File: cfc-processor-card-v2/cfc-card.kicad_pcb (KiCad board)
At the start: 4 copper layers, 99.8 x 94.6 mm, 268 parts, among them J1 ORESAT-DEBUG-CONNECTOR-ALL, J100 DM3BT-DSF-PEJS, J2 J-SAMTEC-TFM-110-X1-XXX-D-RA, J3 CONN_03LONGPADS, J4 TFM-120-01-L-D-RA, Q1 MMBT2907, Q2 PMV45EN, Q3 DMP2240UDM, Q4 PMV45EN, Q5 MOSFET-PCH-SOT23-6, Q6 MOSFET-PCH-SOT23-6, U1 RCLAMP0504FB, U10 TLVH431, U11 TCAN330, U12 MIC842LYC5, U13 MIC842LYC5, U14 MAX4211FETE, U15 TPS62112, U16 MAX7310ATE, U2 DS90CR218AMTD/NOPBMTD48_TEX-L, U3 THGBMJG7C2LBAU8, U4 SN74LVC1G07DCK, U5 TS5A21366, U7 OSD3358-512M-BSM, Y1 24MHz, Y2 ABS07-32.768KHZ-T

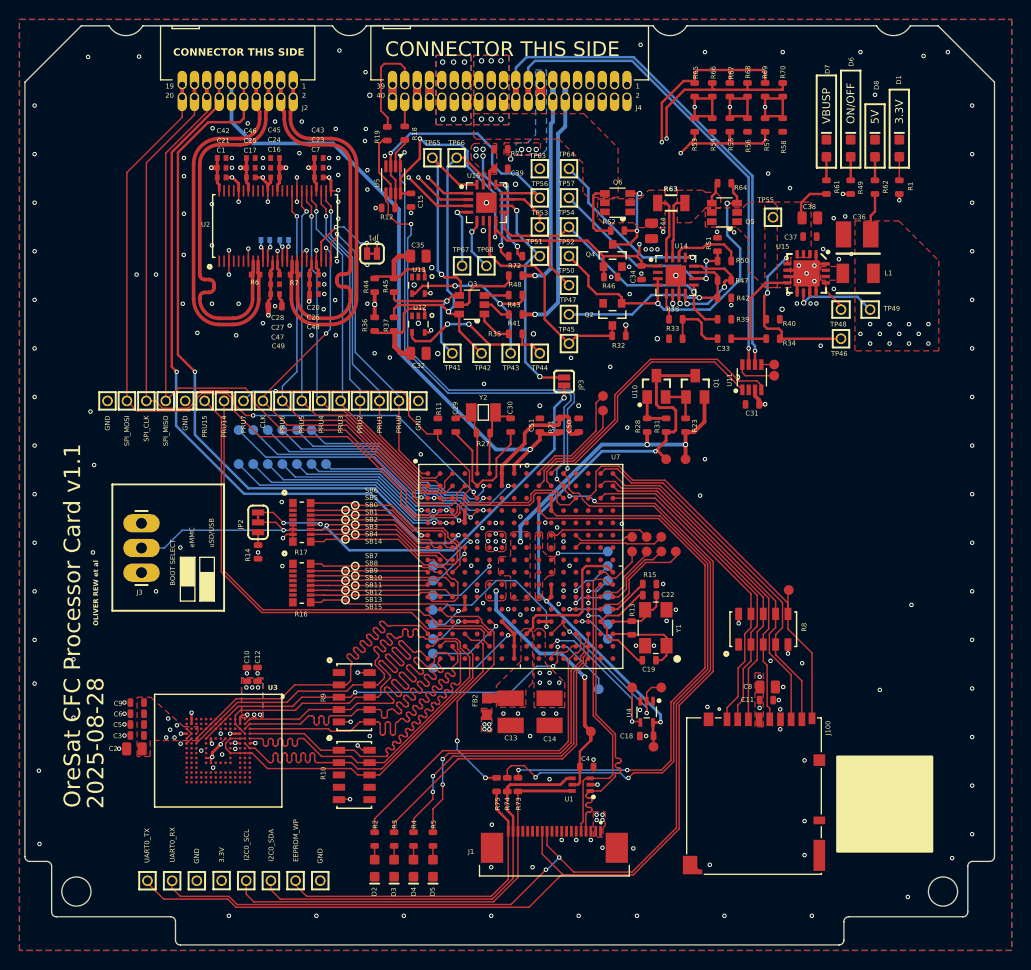
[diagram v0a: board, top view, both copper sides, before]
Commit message: Final polish on schematic and PCB. Cleaned up BOM, fixed github issues which were not really issues. Lots of BOM cleanup, with MPNs and DPNs.
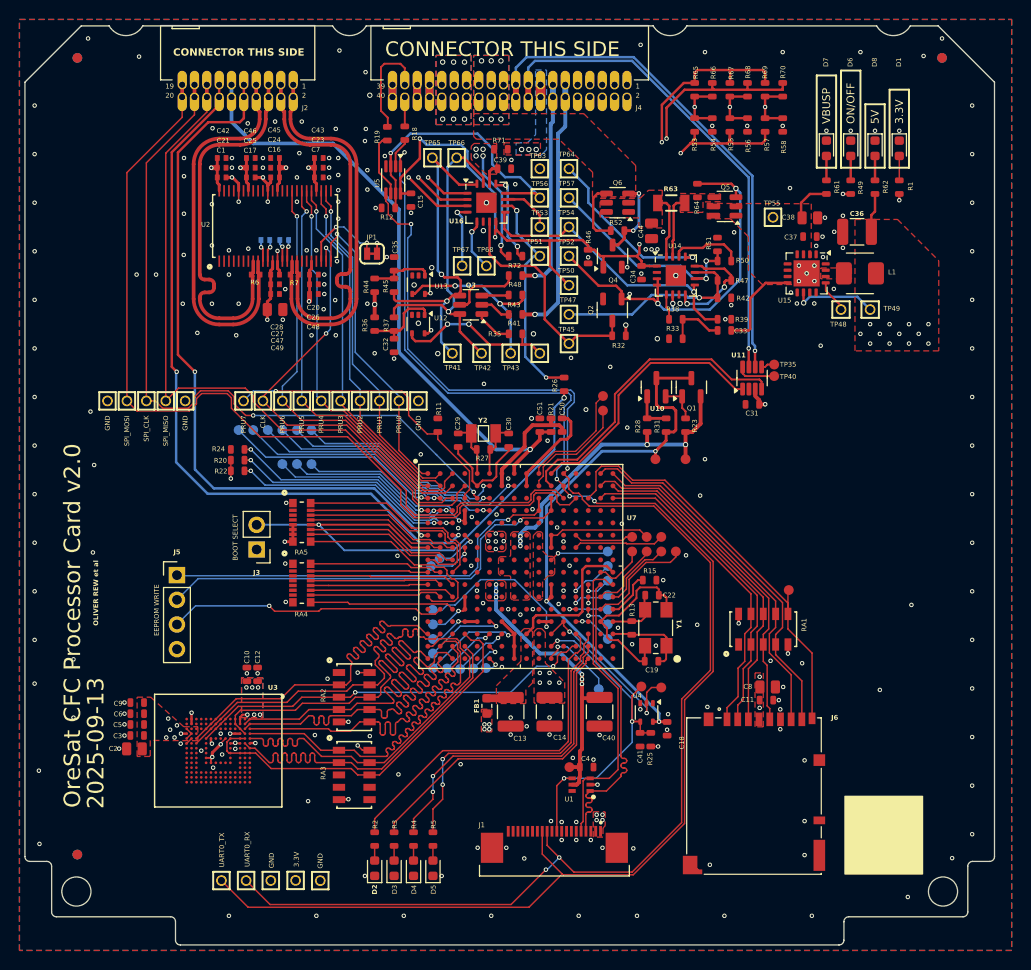
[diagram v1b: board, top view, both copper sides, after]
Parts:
- removed JP2: JUMPER-SMT_3_1-NC_TRACE_SILK, cfc-card:SMT-JUMPER_3_1-NC_TRACE_SILK
- removed JP3: JUMPER-SMT_2_NO_SILK, cfc-card:SMT-JUMPER_2_NO_SILK
- removed R14: DNP, oresat-passives:0603-C-NOSILK
- removed R34: 10k, oresat-passives:0603-C-NOSILK
- removed R40: NP, oresat-passives:0603-C-NOSILK
- removed R73, R74, R75: 100, oresat-passives:0603-C-NOSILK
- removed SB0, SB1, SB10, SB11, SB12, SB13, SB14, SB15, SB2, SB3, SB4, SB5, SB6, SB7, SB8, SB9: TEST-POINT-SMALL, cfc-card:TEST-POINT-SMALL
- removed TP157, TP173: TEST-POINT3X4, cfc-card:PAD.03X.04
- removed TP33, TP34, TP39, TP46, TP70, TP71: TEST-POINT, cfc-card:2MM-TEST-POINT
- added C40: 22u, Capacitor_SMD:C_1210_3225Metric, F.Cu at (157.8, 128.3)
- added C41: 100n, oresat-passives:0603-C-NOSILK, F.Cu at (161.9, 131.2)
- added FID1: Fiducial, Fiducial:Fiducial_1mm_Mask2mm, F.Cu at (104.0, 61.0)
- added FID2: Fiducial, Fiducial:Fiducial_1mm_Mask2mm, F.Cu at (104.0, 143.0)
- added FID3: Fiducial, Fiducial:Fiducial_1mm_Mask2mm, F.Cu at (193.0, 61.0)
- added FID4: Fiducial, Fiducial:Fiducial_1mm_Mask2mm, B.Cu at (104.0, 143.0)
- added FID5: Fiducial, Fiducial:Fiducial_1mm_Mask2mm, B.Cu at (104.0, 61.0)
- added FID6: Fiducial, Fiducial:Fiducial_1mm_Mask2mm, B.Cu at (193.0, 61.0)
- added J5: Conn_01x04, Connector_PinHeader_2.54mm:PinHeader_1x04_P2.54mm_Vertical, F.Cu at (114.2, 114.2)
- added R20: 10k, oresat-passives:0603-C-NOSILK, F.Cu at (120.5, 102.4)
- added R22: 10k, oresat-passives:0603-C-NOSILK, F.Cu at (120.5, 103.5)
- added R24: 10k, oresat-passives:0603-C-NOSILK, F.Cu at (120.5, 101.3)
- added R25: 10k, oresat-passives:0603-C-NOSILK, F.Cu at (163.0, 131.2)
- added R26: 10k, oresat-passives:0603-C-NOSILK, F.Cu at (154.1, 94.6)
- C10, C12, C3, C33, C34, C37, C5, C6, C9: value 1uF -> 1u
- C11, C18, C31, C39, C50: value 0.1uF -> 100n
- C13, C14, C36: value 22uF -> 22u; footprint cfc-card:C1210 -> Capacitor_SMD:C_1210_3225Metric
- C19, C22: value 18pF, 50V -> 10p
- C2, C38, C44, C8: value 10uF -> 10u
- C29, C30: value 18pF, 50V -> 18p
- C32, C35: value 1uF -> 1u; footprint oresat-passives:0805-C-NOSILK -> oresat-passives:0603-C-NOSILK
- C49: footprint oresat-passives:0603-C-NOSILK -> oresat-passives:0805-C-NOSILK
- C51: value 0.1u -> 100n
- D1, D2, D3, D4, D5, D6, D7, D8: footprint cfc-card:LED-0603 -> LED_SMD:LED_0603_1608Metric
- FB1: renamed from FB2; value 30Ω/1.8A -> BLM18KG300JH1D; footprint cfc-card:0603 -> Inductor_SMD:L_0603_1608Metric
- J1: value ORESAT-DEBUG-CONNECTOR-ALL -> 2-1734592-0
- J3: value CONN_03LONGPADS -> Conn_01x02; footprint cfc-card:1X03_LONGPADS -> Connector_PinHeader_2.54mm:PinHeader_1x02_P2.54mm_Vertical
- J6: renamed from J100; footprint cfc-card:DM3BT-DSF-PEJS -> oresat-connectors:J-Hirose-DM3BT-DSF-PEJS
- L1: footprint cfc-card:ECS-MPI4040 -> oresat-passives:L_ECS-MPI4040
- Q1: footprint cfc-card:SOT23-BEC -> Package_TO_SOT_SMD:SOT-23
- Q2, Q4: footprint cfc-card:SOT23 -> Package_TO_SOT_SMD:SOT-23-3
- Q3: footprint cfc-card:SOT23-6 -> Package_TO_SOT_SMD:SOT-23-6
- Q5, Q6: value MOSFET-PCH-SOT23-6 -> DMP3050LVT-7; footprint cfc-card:SOT23-6 -> Package_TO_SOT_SMD:TSOT-23-6
- R11: value DNP -> 10k
- R27: value DNP -> 1M
- R29, R30: value NP -> 100
- R42: value NP -> 10k
- RA4: renamed from R16; value 100k -> 47k
- RA5: renamed from R17; value 100k -> 47k
- TP14: moved to B.Cu
- U10: footprint cfc-card:SOT23-3 -> Package_TO_SOT_SMD:SOT-23
- U11: footprint cfc-card:SOT23-8_TI-DCN -> Package_TO_SOT_SMD:SOT-23-8
- U12, U13: footprint cfc-card:SC70-5 -> Package_TO_SOT_SMD:SOT-353_SC-70-5
- U14: footprint cfc-card:QFN65P400X400X80-17T210 -> Package_DFN_QFN:QFN-16-1EP_4x4mm_P0.65mm_EP2.1x2.1mm
- U15: footprint cfc-card:S-PVQFN-16 -> Package_DFN_QFN:Texas_RSA_VQFN-16-1EP_4x4mm_P0.65mm_EP2.7x2.7mm
- U16: value MAX7310ATE -> MAX7310ATE+; footprint cfc-card:QFN65P400X400X80-17T210 -> Package_DFN_QFN:QFN-16-1EP_4x4mm_P0.65mm_EP2.1x2.1mm
- U2: value DS90CR218AMTD/NOPBMTD48_TEX-L -> DS90CR218AMTD/NOPB
- U3: value THGBMJG7C2LBAU8 -> SFEM016GB1EA1TO-I-GE-121-STD
- U4: value SN74LVC1G07DCK -> SN74AUC1G07DCKR; footprint cfc-card:C70(TI-DCK) -> Package_TO_SOT_SMD:SOT-353_SC-70-5
- U7: value OSD3358-512M-BSM -> OSD3358-1G-ISM; footprint cfc-card:OSD335X-BGA-256 -> oresat-ics:U-Octavo-OSD335X-BGA-256
- Y1: value 24MHz -> ECS-240-12-30BQ-AEN-TR; footprint cfc-card:5X3.2-4SMD -> oresat-passives:CRYSTAL-5X3.2-4SMD
- Y2: footprint cfc-card:CRYSTAL_3.2X1.5 -> oresat-passives:CRYSTAL_3.2X1.5
- moved TP10 32.0 mm to (144.8, 123.8), turned to 0 degrees
- moved TP11 31.8 mm to (146.1, 123.8), turned to 0 degrees
- moved TP9 28.0 mm to (142.1, 123.8), turned to 0 degrees
- moved TP14 21.4 mm to (143.4, 123.9), turned to 0 degrees
- moved J3 12.2 mm to (122.5, 111.6), turned to 180 degrees
- moved TP32 7.61 mm to (118.8, 145.7)
- moved TP78 7.61 mm to (123.9, 145.7)
- moved TP2 7.61 mm to (126.5, 145.7)
- moved TP31 7.61 mm to (121.4, 145.7)
- moved TP3 4.27 mm to (154.7, 134.0)
- moved R46 3.13 mm to (156.6, 81.5), turned to 90 degrees
- moved R64 2.88 mm to (167.8, 74.7), turned to -90 degrees
- moved C32 2.63 mm to (136.6, 90.6), turned to -90 degrees
- moved C35 2.62 mm to (136.6, 82.2), turned to 90 degrees
- moved C18 2.23 mm to (164.7, 130.1), turned to -90 degrees
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- renumbered R8 to RA1, R9 to RA2, R10 to RA3
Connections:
- net /OSD3358: SIP A + E + F (PWR)/PMIC_PGOOD renamed /OSD3358: SIP A (PWR)/PMIC_PGOOD
- net /OSD3358: SIP C (SD, eMMC)/EMMC_CLK renamed /OSD3358: SIP C (SD, eMMC, PRU)/EMMC_CLK
- net /OSD3358: SIP C (SD, eMMC)/EMMC_CMD renamed /OSD3358: SIP C (SD, eMMC, PRU)/EMMC_CMD
- net /OSD3358: SIP C (SD, eMMC)/PRU_BUS.PRU0_0 renamed /OSD3358: SIP C (SD, eMMC, PRU)/PRU_BUS.PRU0_0
- net /OSD3358: SIP C (SD, eMMC)/PRU_BUS.PRU0_1 renamed /OSD3358: SIP C (SD, eMMC, PRU)/PRU_BUS.PRU0_1
- net /OSD3358: SIP C (SD, eMMC)/PRU_BUS.PRU0_2 renamed /OSD3358: SIP C (SD, eMMC, PRU)/PRU_BUS.PRU0_2
- net /OSD3358: SIP C (SD, eMMC)/PRU_BUS.PRU0_3 renamed /OSD3358: SIP C (SD, eMMC, PRU)/PRU_BUS.PRU0_3
- net /OSD3358: SIP C (SD, eMMC)/PRU_BUS.PRU0_4 renamed /OSD3358: SIP C (SD, eMMC, PRU)/PRU_BUS.PRU0_4
- net /OSD3358: SIP C (SD, eMMC)/PRU_BUS.PRU0_5 renamed /OSD3358: SIP C (SD, eMMC, PRU)/PRU_BUS.PRU0_5
- net /OSD3358: SIP C (SD, eMMC)/PRU_BUS.PRU0_6 renamed /OSD3358: SIP C (SD, eMMC, PRU)/PRU_BUS.PRU0_6
- net /OSD3358: SIP C (SD, eMMC)/PRU_BUS.PRU0_7 renamed /OSD3358: SIP C (SD, eMMC, PRU)/PRU_BUS.PRU0_7
- net /OSD3358: SIP C (SD, eMMC)/PRU_BUS.PRU_16_CLK renamed /OSD3358: SIP C (SD, eMMC, PRU)/PRU_BUS.PRU_16_CLK
- net /OSD3358: SIP C (SD, eMMC)/~{EMMC_RST} renamed /OSD3358: SIP C (SD, eMMC, PRU)/~{EMMC_RST}
- net /Power (OPD)/BOOT0 renamed Net-(U16-IO5)
- net Net-(R10-11) renamed /OSD3358: SIP C (SD, eMMC, PRU)/EMMC_D1
- net Net-(R10-22) renamed /OSD3358: SIP C (SD, eMMC, PRU)/EMMC_D7
- net Net-(R10-88) renamed /OSD3358: SIP C (SD, eMMC, PRU)/EMMC_D6
- net Net-(R10-99) renamed /OSD3358: SIP C (SD, eMMC, PRU)/EMMC_D2
- net Net-(R9-44) renamed /OSD3358: SIP C (SD, eMMC, PRU)/EMMC_D3
- net Net-(R9-66) renamed /OSD3358: SIP C (SD, eMMC, PRU)/EMMC_D0
- net Net-(R9-77) renamed /OSD3358: SIP C (SD, eMMC, PRU)/EMMC_D4
- net Net-(R9-88) renamed /OSD3358: SIP C (SD, eMMC, PRU)/EMMC_D5
- net Net-(U7A-I2C0_SCL) renamed /OSD3358: SIP A (PWR)/I2C0_SCL
- net Net-(U7A-I2C0_SDA) renamed /OSD3358: SIP A (PWR)/I2C0_SDA
- C18 pad 1: /OSD3358: SIP A + E + F (PWR)/N$118 -> Net-(Q1-C)
- C50 pad 2: GND -> Net-(U7B-AGND_ADC)
- J1 pad 10: unconnected-(J1-NRST-Pad10) -> nRESET
- J1 pad 18: I2C0_SCL -> unconnected-(J1-DEBUG-1-Pad18)
- J1 pad 19: I2C0_SDA -> unconnected-(J1-DEBUG-2-Pad19)
- J1 pad 20: EEPROM_WP -> unconnected-(J1-DEBUG-3-Pad20)
- J3 pad 1: 3.3V -> GND
- R1 pad 2: Net-(D1-PadA) -> Net-(D1-A)
- R2 pad 2: Net-(D2-PadA) -> Net-(D2-A)
- R23 pad 1: Net-(U10-CATHODE) -> Net-(Q1-B)
- R3 pad 2: Net-(D3-PadA) -> Net-(D3-A)
- R31 pad 1: /OSD3358: SIP A + E + F (PWR)/N$118 -> Net-(Q1-C)
- R4 pad 2: Net-(D4-PadA) -> Net-(D4-A)
- R49 pad 1: Net-(D6-PadA) -> Net-(D6-A)
- R5 pad 2: Net-(D5-PadA) -> Net-(D5-A)
- R61 pad 1: Net-(D7-PadA) -> Net-(D7-A)
- R62 pad 1: Net-(D8-PadA) -> Net-(D8-A)
- RA5 pad 12: Net-(JP2-Pad3) -> SYSBOOT2
- TP109 pad P$1: /OSD3358: SIP A + E + F (PWR)/RESET# -> nRESET
- TP14 pad P$1: /OSD3358: SIP A + E + F (PWR)/N$118 -> Net-(TP14-1)
- TP164 pad P$1: /OSD3358: SIP A + E + F (PWR)/N$118 -> Net-(Q1-C)
- U1 pad 4: I2C0_SDA -> nRESET
- U1 pad 6: I2C0_SCL -> unconnected-(U1-I4-Pad6)
- U10 pad 2: Net-(U10-CATHODE) -> Net-(Q1-B)
- U10 pad 3: /OSD3358: SIP A + E + F (PWR)/N$118 -> Net-(Q1-C)
- U12 pad 3: (no net) -> unconnected-(U12-Pad3)
- U13 pad 3: (no net) -> unconnected-(U13-Pad3)
- U14 pad 2: (no net) -> unconnected-(U14-IN_(NC)-Pad2)
- U15 pad 5: Net-(U15-SYNC) -> GND
- U2 pad 6: (no net) -> unconnected-(U2-Pad6)
- U4 pad 1: (no net) -> unconnected-(U4-Pad1)
- U4 pad 4: /OSD3358: SIP A + E + F (PWR)/RESET# -> nRESET
- U4 pad 5: /OSD3358: SIP A + E + F (PWR)/N$118 -> Net-(Q1-C)
- U7 pad A9: GND -> Net-(U7B-AGND_ADC)
- U7 pad B9: GND -> Net-(U7B-AGND_ADC)
- U7 pad D3: Net-(TP9-1) -> Net-(U7B-TRSTN)
- U7 pad D5: Net-(TP173-1) -> unconnected-(U7F-CAP_VDD_RTC-PadD5)
- U7 pad E2: Net-(TP10-1) -> Net-(U7B-EMU0)
- U7 pad E3: Net-(TP11-1) -> Net-(U7B-EMU1)
- U7 pad H6: Net-(TP157-1) -> unconnected-(U7F-VPP-PadH6)
- U7 pad K11: /OSD3358: SIP A + E + F (PWR)/N$118 -> Net-(Q1-C)
- U7 pad L11: /OSD3358: SIP A + E + F (PWR)/N$118 -> Net-(Q1-C)
- U7 pad M2: Net-(U7A-EEPROM_WP) -> /OSD3358: SIP A (PWR)/EEPROM_WP
- U7 pad P6: /OSD3358: SIP C (SD, eMMC)/PRU_BUS.PRU0_14 -> Net-(TP9-1)
- U7 pad P7: unconnected-(U7C-GPMC_AD15-PadP7) -> Net-(TP14-1)
- U7 pad R11: /OSD3358: SIP A + E + F (PWR)/RESET# -> nRESET
- U7 pad R6: /OSD3358: SIP C (SD, eMMC)/PRU_BUS.PRU0_15 -> Net-(TP10-1)
- U7 pad T6: unconnected-(U7C-GPMC_AD14-PadT6) -> Net-(TP11-1)
- Y1 pad 2: GND -> /OSD3358: SIP B (USB, XTAL, ADC)/OSC0_GND
- Y1 pad 4: GND -> /OSD3358: SIP B (USB, XTAL, ADC)/OSC0_GND
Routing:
- net /OSD3358: SIP A + E + F (PWR)/N$118: track 62.5 -> 0.00 mm, vias 3 -> 0
- net Net-(Q1-C): track 0.00 -> 58.9 mm, vias 0 -> 3
- net /OSD3358: SIP C (SD, eMMC)/PRU_BUS.PRU0_15: track 49.6 -> 0.00 mm
- net /OSD3358: SIP C (SD, eMMC)/PRU_BUS.PRU0_14: track 47.7 -> 0.00 mm
- net I2C0_SCL: track 45.2 -> 0.00 mm
- net I2C0_SDA: track 43.8 -> 0.00 mm
- net nRESET: track 0.00 -> 37.8 mm, vias 0 -> 3
- net EEPROM_WP: track 33.1 -> 0.00 mm
- net GND: track 51.1 -> 18.6 mm, vias 260 -> 278
- net /OSD3358: SIP A (PWR)/EEPROM_WP: track 0.00 -> 28.7 mm, vias 0 -> 1
- net Net-(U7A-EEPROM_WP): track 25.6 -> 0.00 mm, vias 2 -> 0
- net Net-(U7B-TRSTN): track 0.00 -> 24.6 mm, vias 0 -> 2
- net Net-(U7B-EMU1): track 0.00 -> 24.2 mm, vias 0 -> 2
- net Net-(U7B-EMU0): track 0.00 -> 22.4 mm, vias 0 -> 2
- net Net-(TP11-1): track 23.2 -> 2.03 mm
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- removed copper zone on F.Cu, net Net-(TP161-1)
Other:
- board text added: "EEPROM WRITE"
- board text removed: "EEPROM_WP"
- board text removed: "I2C0_SCL"
- board text removed: "I2C0_SDA"
- board text removed: "PRU14"
- board text removed: "PRU15"
- board text removed: "eMMC"
- board text removed: "uSD/USB"

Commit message: Updated mfg date. More stiching. More layout tweaking. Done.
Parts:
- moved TP48 1.63 mm to (181.1, 87.4)
- moved C38 0.84 mm to (179.4, 78.3)
- moved TP49 0.64 mm to (185.2, 86.5)
- moved C37 0.37 mm to (179.5, 79.8)
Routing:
- net 5V: track 12.6 -> 11.3 mm, vias 18 -> 16
- net VBUSP: track 14.3 -> 15.1 mm
- net /OSD3358: SIP C (SD, eMMC, PRU)/~{EMMC_RST}: track 42.4 -> 43.1 mm
- net Net-(U15-PG): track 3.40 -> 3.25 mm, vias 0 -> 1
- net GND: vias 278 -> 311
